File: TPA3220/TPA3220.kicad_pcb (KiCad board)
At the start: 2 copper layers, 84 x 70 mm, 24 parts, among them IC1 ESP32-WROOM-32UE-N8R2, IC2 RESET, IC3 BOOT, J4 PROG, U1 TPA3220DDWR, U2 LD1117, U3 PCM5242RHBR

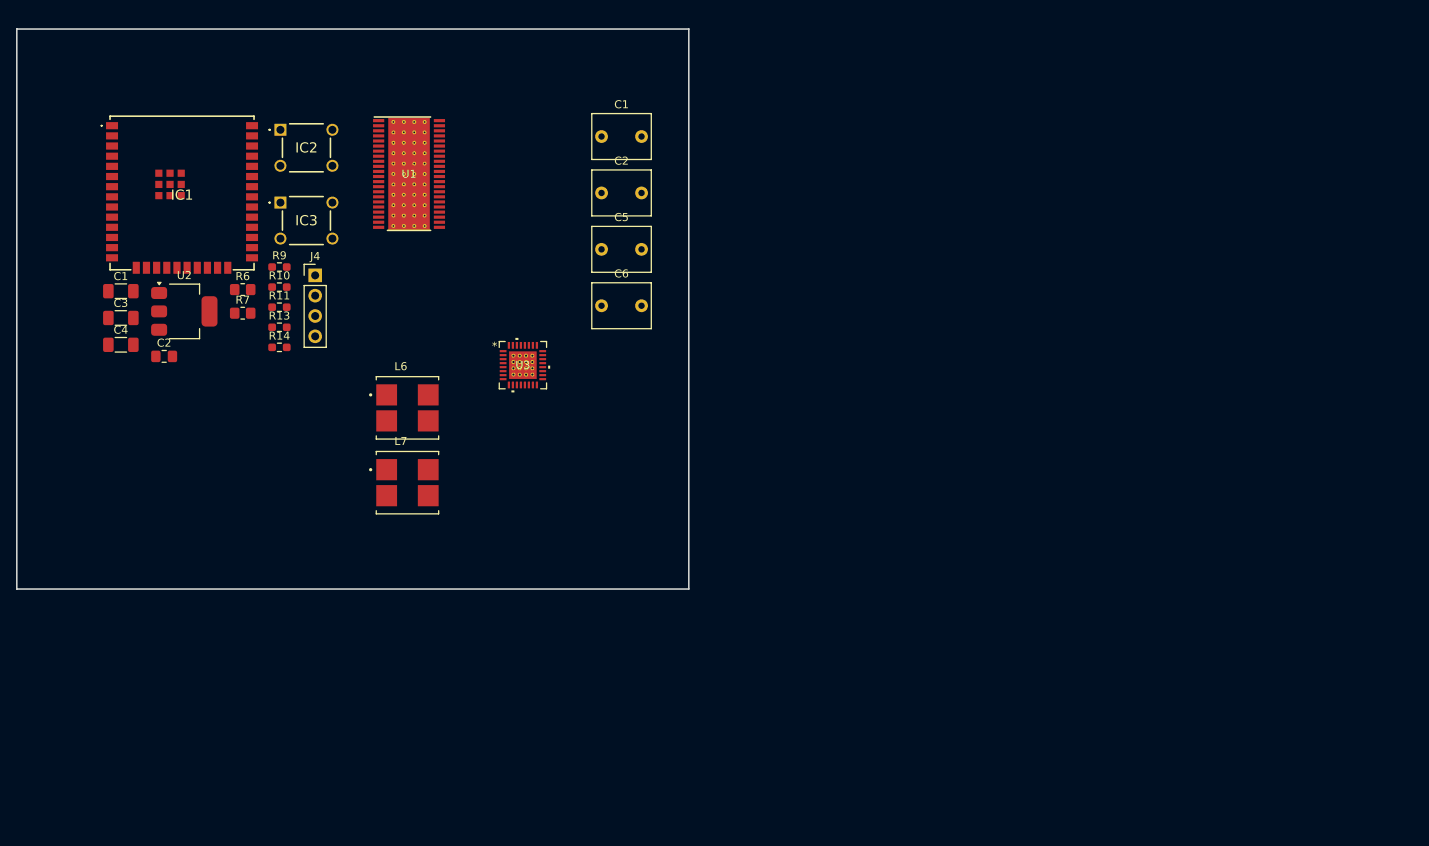
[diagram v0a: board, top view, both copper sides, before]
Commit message: TPA3220: snapshot before agent schematic completion
Co-Authored-By: Claude Opus 5.5 <noreply@anthropic.com>
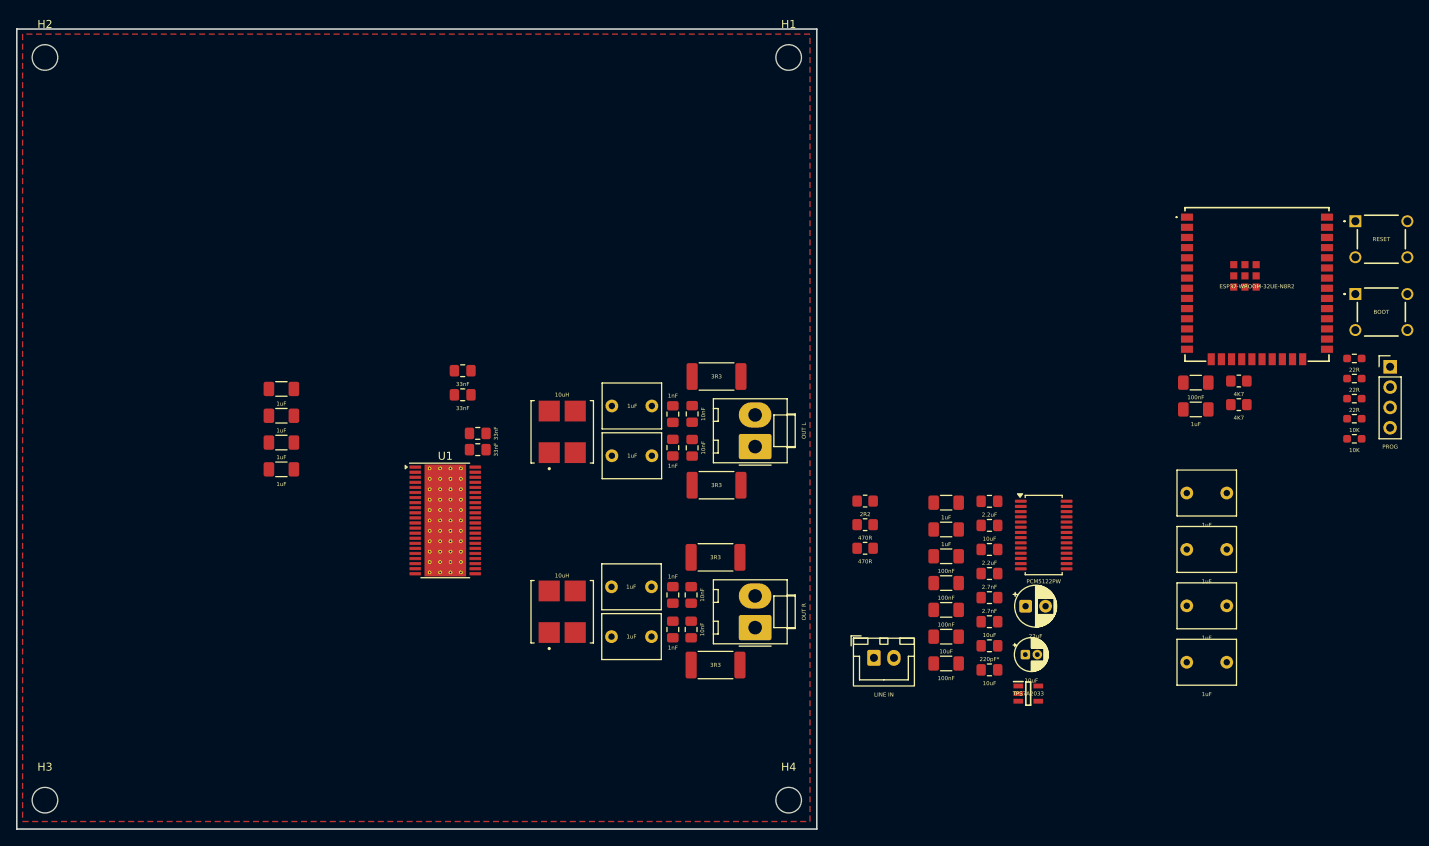
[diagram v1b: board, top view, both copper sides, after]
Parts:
- removed the C1 at (113.2, 91.2)
- removed the C1 at (173.3, 71.9)
- removed the C2 at (118.7, 99.3)
- removed the C2 at (173.3, 78.9)
- removed U3: PCM5242RHBR, Custom:PCM5242
- added C1: 1uF, Capacitor_THT:C_Rect_L7.2mm_W5.5mm_P5.00mm_FKS2_FKP2_MKS2_MKP2, F.Cu at (246.5, 116.4)
- added C10: 22uF, Capacitor_THT:CP_Radial_D5.0mm_P2.50mm, F.Cu at (226.3, 130.6)
- added C11: 100nF, Capacitor_SMD:C_1206_3216Metric_Pad1.33x1.80mm_HandSolder, F.Cu at (216.4, 124.3)
- added C12: 2.2uF, Capacitor_SMD:C_0805_2012Metric_Pad1.18x1.45mm_HandSolder, F.Cu at (221.8, 117.5)
- added C13: 10uF, Capacitor_SMD:C_0805_2012Metric_Pad1.18x1.45mm_HandSolder, F.Cu at (221.8, 120.5)
- added C14: 2.2uF, Capacitor_SMD:C_0805_2012Metric_Pad1.18x1.45mm_HandSolder, F.Cu at (221.8, 123.5)
- added C15: 100nF, Capacitor_SMD:C_1206_3216Metric_Pad1.33x1.80mm_HandSolder, F.Cu at (216.4, 127.7)
- added C16: 2.7nF, Capacitor_SMD:C_0805_2012Metric_Pad1.18x1.45mm_HandSolder, F.Cu at (221.8, 126.5)
- added C17: 100nF, Capacitor_SMD:C_1206_3216Metric_Pad1.33x1.80mm_HandSolder, F.Cu at (216.4, 131.0)
- added C18: 10uF, Capacitor_SMD:C_1206_3216Metric_Pad1.33x1.80mm_HandSolder, F.Cu at (216.4, 134.4)
- added C19: 2.7nF, Capacitor_SMD:C_0805_2012Metric_Pad1.18x1.45mm_HandSolder, F.Cu at (221.8, 129.5)
- added C2: 1uF, Capacitor_THT:C_Rect_L7.2mm_W5.5mm_P5.00mm_FKS2_FKP2_MKS2_MKP2, F.Cu at (246.5, 123.5)
- added C20: 10uF, Capacitor_SMD:C_0805_2012Metric_Pad1.18x1.45mm_HandSolder, F.Cu at (221.8, 132.5)
- added C21: 220pF*, Capacitor_SMD:C_0805_2012Metric_Pad1.18x1.45mm_HandSolder, F.Cu at (221.8, 135.5)
- added C22: 100nF, Capacitor_SMD:C_1206_3216Metric_Pad1.33x1.80mm_HandSolder, F.Cu at (216.4, 137.7)
- added C23: 10uF, Capacitor_SMD:C_0805_2012Metric_Pad1.18x1.45mm_HandSolder, F.Cu at (221.8, 138.5)
- added C24: 33nF, Capacitor_SMD:C_0805_2012Metric_Pad1.18x1.45mm_HandSolder, F.Cu at (157.9, 111.0)
- added C25: 33nF, Capacitor_SMD:C_0805_2012Metric_Pad1.18x1.45mm_HandSolder, F.Cu at (157.9, 109.0)
- added C26: 33nF, Capacitor_SMD:C_0805_2012Metric_Pad1.18x1.45mm_HandSolder, F.Cu at (156.0, 101.1)
- added C27: 33nF, Capacitor_SMD:C_0805_2012Metric_Pad1.18x1.45mm_HandSolder, F.Cu at (156.0, 104.1)
- added C28: 1uF, Capacitor_THT:C_Rect_L7.2mm_W5.5mm_P5.00mm_FKS2_FKP2_MKS2_MKP2, F.Cu at (174.6, 111.8)
- added C29: 1uF, Capacitor_THT:C_Rect_L7.2mm_W5.5mm_P5.00mm_FKS2_FKP2_MKS2_MKP2, F.Cu at (179.6, 105.5)
- added C30: 1nF, Capacitor_SMD:C_0805_2012Metric_Pad1.18x1.45mm_HandSolder, F.Cu at (182.2, 110.7)
- added C31: 1nF, Capacitor_SMD:C_0805_2012Metric_Pad1.18x1.45mm_HandSolder, F.Cu at (182.2, 106.6)
- added C32: 10nF, Capacitor_SMD:C_0805_2012Metric_Pad1.18x1.45mm_HandSolder, F.Cu at (184.7, 110.8)
- added C33: 10nF, Capacitor_SMD:C_0805_2012Metric_Pad1.18x1.45mm_HandSolder, F.Cu at (184.7, 106.5)
- added C34: 1uF, Capacitor_THT:C_Rect_L7.2mm_W5.5mm_P5.00mm_FKS2_FKP2_MKS2_MKP2, F.Cu at (174.6, 134.4)
- added C35: 1uF, Capacitor_THT:C_Rect_L7.2mm_W5.5mm_P5.00mm_FKS2_FKP2_MKS2_MKP2, F.Cu at (179.6, 128.1)
- added C36: 1nF, Capacitor_SMD:C_0805_2012Metric_Pad1.18x1.45mm_HandSolder, F.Cu at (182.2, 133.5)
- added C37: 1nF, Capacitor_SMD:C_0805_2012Metric_Pad1.18x1.45mm_HandSolder, F.Cu at (182.2, 129.2)
- added C38: 10nF, Capacitor_SMD:C_0805_2012Metric_Pad1.18x1.45mm_HandSolder, F.Cu at (184.5, 133.5)
- added C39: 10nF, Capacitor_SMD:C_0805_2012Metric_Pad1.18x1.45mm_HandSolder, F.Cu at (184.5, 129.2)
- added C40: 1uF, Capacitor_SMD:C_1206_3216Metric_Pad1.33x1.80mm_HandSolder, F.Cu at (133.3, 103.4)
- added C41: 1uF, Capacitor_SMD:C_1206_3216Metric_Pad1.33x1.80mm_HandSolder, F.Cu at (133.3, 106.8)
- added C42: 1uF, Capacitor_SMD:C_1206_3216Metric_Pad1.33x1.80mm_HandSolder, F.Cu at (133.3, 110.1)
- added C43: 1uF, Capacitor_SMD:C_1206_3216Metric_Pad1.33x1.80mm_HandSolder, F.Cu at (133.3, 113.5)
- added C7: 10uF, Capacitor_THT:CP_Radial_D4.0mm_P1.50mm, F.Cu at (226.3, 136.6)
- added C8: 1uF, Capacitor_SMD:C_1206_3216Metric_Pad1.33x1.80mm_HandSolder, F.Cu at (216.4, 117.6)
- added C9: 1uF, Capacitor_SMD:C_1206_3216Metric_Pad1.33x1.80mm_HandSolder, F.Cu at (216.4, 121.0)
- added H1: MountingHole, MountingHole:MountingHole_3.2mm_M3, F.Cu at (196.7, 62.0)
- added H2: MountingHole, MountingHole:MountingHole_3.2mm_M3, F.Cu at (103.8, 62.0)
- added H3: MountingHole, MountingHole:MountingHole_3.2mm_M3, F.Cu at (103.8, 154.8)
- added H4: MountingHole, MountingHole:MountingHole_3.2mm_M3, F.Cu at (196.7, 154.8)
- added IC4: TPS7A2033, Custom:SOT95P280X145-5N, F.Cu at (226.7, 141.5)
- added J1: LINE IN, Connector_JST:JST_XH_B2B-XH-A_1x02_P2.50mm_Vertical, F.Cu at (207.4, 137.0)
- added J16: OUT L, Connector_Molex:Molex_KK-396_A-41791-0002_1x02_P3.96mm_Vertical, F.Cu at (192.5, 110.6)
- added J17: OUT R, Connector_Molex:Molex_KK-396_A-41791-0002_1x02_P3.96mm_Vertical, F.Cu at (192.5, 133.2)
- added R1: 2R2, Resistor_SMD:R_0805_2012Metric_Pad1.20x1.40mm_HandSolder, F.Cu at (206.3, 117.4)
- added R18: 3R3, Resistor_SMD:R_2512_6332Metric_Pad1.40x3.35mm_HandSolder, F.Cu at (187.7, 115.4)
- added R19: 3R3, Resistor_SMD:R_2512_6332Metric_Pad1.40x3.35mm_HandSolder, F.Cu at (187.7, 101.9)
- added R2: 470R, Resistor_SMD:R_0805_2012Metric_Pad1.20x1.40mm_HandSolder, F.Cu at (206.3, 120.4)
- added R20: 3R3, Resistor_SMD:R_2512_6332Metric_Pad1.40x3.35mm_HandSolder, F.Cu at (187.6, 137.9)
- added R21: 3R3, Resistor_SMD:R_2512_6332Metric_Pad1.40x3.35mm_HandSolder, F.Cu at (187.6, 124.5)
- added R3: 470R, Resistor_SMD:R_0805_2012Metric_Pad1.20x1.40mm_HandSolder, F.Cu at (206.3, 123.3)
- U1: footprint Custom:TPA3220 -> TPA3220:TPA3220_DDW0044D_HTSSOP-44_6.1x14mm_P0.635mm_EP5.2x14mm_Mask4.43x7.3mm_ThermalVias
- U2: value LD1117 -> PCM5122PW; footprint Package_TO_SOT_SMD:SOT-223-3_TabPin2 -> Package_SO:TSSOP-28_4.4x9.7mm_P0.65mm
- moved IC2 134.9 mm to (267.6, 82.4)
- moved IC3 134.9 mm to (267.6, 91.5)
- moved R10 134.9 mm to (267.4, 102.1)
- moved R11 134.9 mm to (267.4, 104.6)
- moved R13 134.9 mm to (267.4, 107.1)
- moved R14 134.9 mm to (267.4, 109.6)
- moved R9 134.9 mm to (267.4, 99.6)
- moved IC1 134.9 mm to (255.3, 90.6)
- moved J4 134.9 mm to (271.9, 100.6)
- moved C3 134.6 mm to (247.6, 102.6)
- moved C4 134.6 mm to (247.6, 106.0)
- moved R6 125.0 mm to (253.0, 102.4)
- moved R7 125.0 mm to (253.0, 105.4)
- moved U2 111.0 mm to (228.6, 121.7)
- moved C5 85.7 mm to (246.5, 130.5)
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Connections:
- L6 pad 1: Net-(L6-Pad1) -> Net-(U1-OUT1_M)
- L6 pad 2: unconnected-(L6-Pad2) -> Net-(J16-Pin_1)
- L6 pad 3: unconnected-(L6-Pad3) -> Net-(J16-Pin_2)
- L6 pad 4: Net-(U1-OUT1_M) -> Net-(C24-Pad2)
- L7 pad 1: Net-(U1-OUT2_P) -> Net-(C27-Pad2)
- L7 pad 2: unconnected-(L7-Pad2) -> Net-(J17-Pin_1)
- L7 pad 3: unconnected-(L7-Pad3) -> Net-(J17-Pin_2)
- L7 pad 4: Net-(L7-Pad4) -> Net-(U1-OUT2_P)
- U1 pad 23: unconnected-(U1-BST2_M-Pad23) -> Net-(U1-BST2_M)
- U1 pad 24: unconnected-(U1-BST2_P-Pad24) -> Net-(U1-BST2_P)
- U1 pad 27: Net-(L7-Pad4) -> Net-(C27-Pad2)
- U1 pad 28: Net-(L7-Pad4) -> Net-(C27-Pad2)
- U1 pad 29: unconnected-(U1-PVDD-Pad29) -> /AMP/PVDD
- U1 pad 30: unconnected-(U1-PVDD-Pad30) -> /AMP/PVDD
- U1 pad 31: unconnected-(U1-PVDD-Pad31) -> /AMP/PVDD
- U1 pad 36: unconnected-(U1-PVDD-Pad36) -> /AMP/PVDD
- U1 pad 37: unconnected-(U1-PVDD-Pad37) -> /AMP/PVDD
- U1 pad 38: unconnected-(U1-PVDD-Pad38) -> /AMP/PVDD
- U1 pad 39: Net-(L6-Pad1) -> Net-(C24-Pad2)
- U1 pad 40: Net-(L6-Pad1) -> Net-(C24-Pad2)
- U1 pad 43: unconnected-(U1-BST1_M-Pad43) -> Net-(U1-BST1_M)
- U1 pad 44: unconnected-(U1-BST1_P-Pad44) -> Net-(U1-BST1_P)
- U2 pad 1: GND -> /DAC/AVDD
- U2 pad 2: /ESP32/3V3-ESP -> Net-(U2-CAPP)
- U2 pad 3: /ESP32/5V -> GND
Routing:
- added copper zone on F.Cu, net GND
- added copper zone on In1.Cu, net GND
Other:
- board size 84 x 70 mm -> 100 x 100 mm
- copper layers 2 -> 4
